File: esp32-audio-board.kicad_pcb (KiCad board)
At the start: 4 copper layers, 37.5 x 70 mm, 125 parts, among them IC1 LP2985A-33DBVR, J1 EN_PAD0, J10 PWR_LED+, J11 HP_LOUT1, J12 HP_ROUT1, J13 HP_LOUT2, J14 HP_ROUT2, J15 MIC_LIN1, J16 MIC_LIN1_GND, J17 MIC_RIN1, J18 MIC_RIN1_GND, J19 HP_GND1, J2 JST S2B, J20 HP_GND2, J21 VP_PAD0, J22 PWR_LED-, J23 CHG_LED+, J24 CHG_LED-, J3 USB_C_Receptacle_USB2.0_16P, J4 EN_PAD1, J5 VP_PAD1, J6 VN_PAD0, J7 VN_PAD1, J8 IO34_PAD0, J9 IO34_PAD1, Q1 SS8050, Q2 SS8050, Q4 AO3401A, U1 ESP32-WROOM-32E, U2 CP2102, U3 MCP73831-2-OT, U5 ES8388

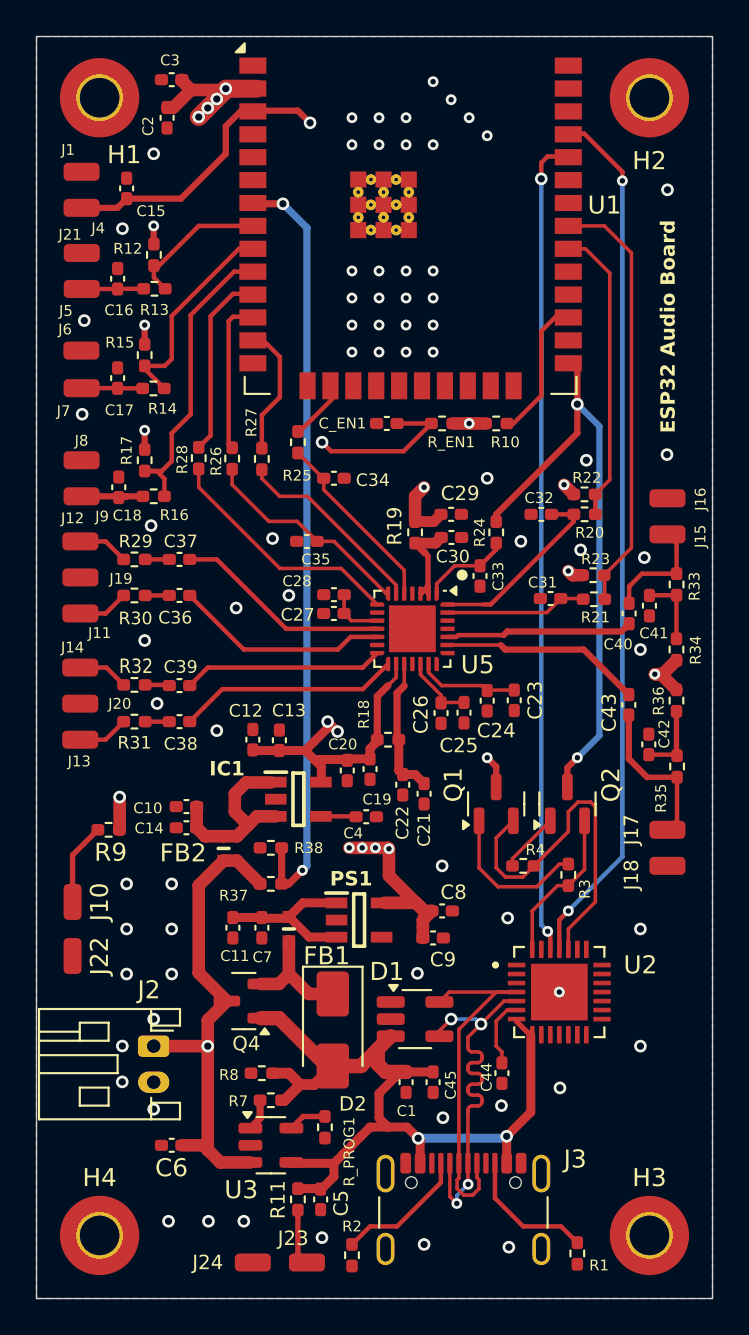
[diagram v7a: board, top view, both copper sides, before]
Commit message: esp32-audio-board: fix GND plane for EN cap
The capacitor close to the ESP module was cutting
the GND pour narrow to about 0.3mm, which can be
too narrow for a stable GND signal to pass. Moved
some traces around it and added many GND viases for
caps and resistors to allow for shorter GND routes.

Signed-off-by: RaresCon <rares.constantin2002@gmail.com>
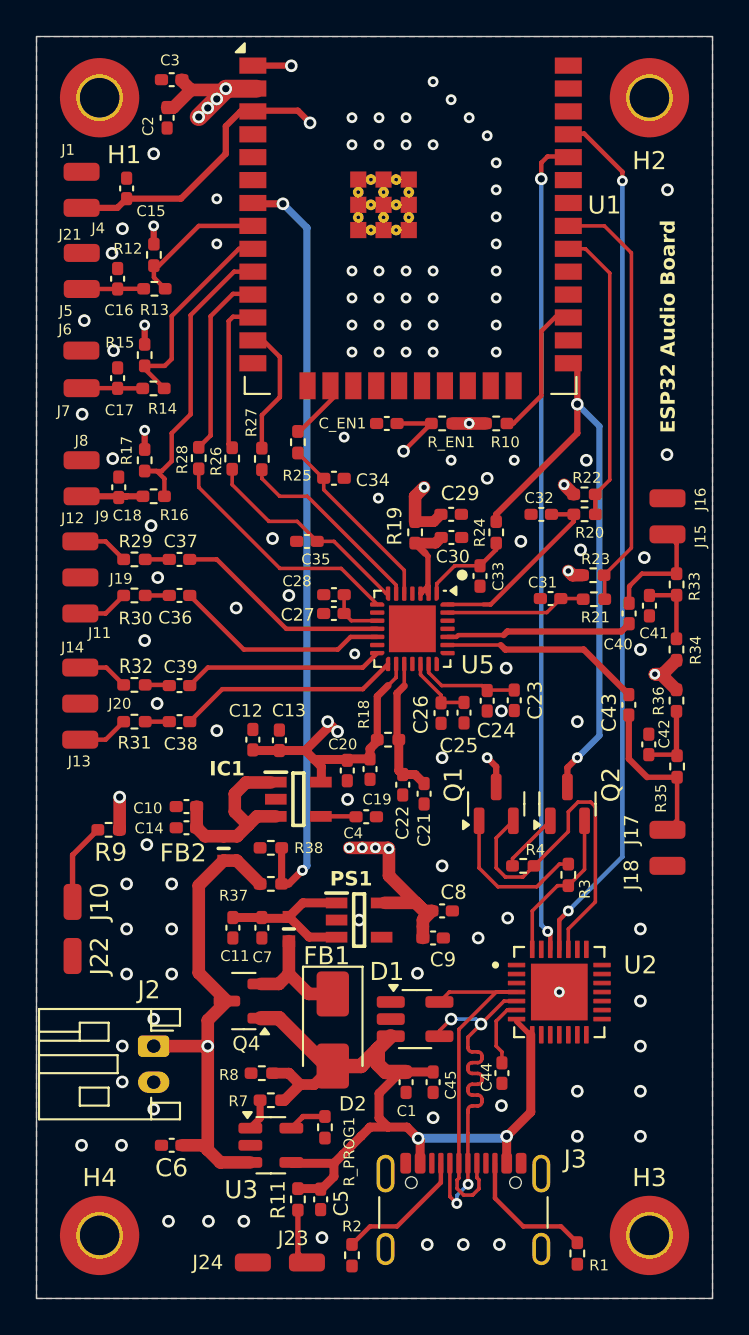
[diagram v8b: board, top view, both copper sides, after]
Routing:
- net GND: track 0.71 -> 2.84 mm, vias 71 -> 106
